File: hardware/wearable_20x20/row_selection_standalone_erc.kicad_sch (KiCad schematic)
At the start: 76 parts, among them Q201 AO3403, Q202 AO3403, Q203 AO3403, Q204 AO3403, Q205 AO3403, Q206 AO3403, Q207 AO3403, Q208 AO3403, Q209 AO3403, Q210 AO3403, Q211 AO3403, Q212 AO3403, Q213 AO3403, Q214 AO3403, Q215 AO3403, Q216 AO3403, Q217 AO3403, Q218 AO3403, Q219 AO3403, Q220 AO3403, U201 SN74LVC8T245RHLR, U202 74HC154PW,118, U203 74HC154PW,118

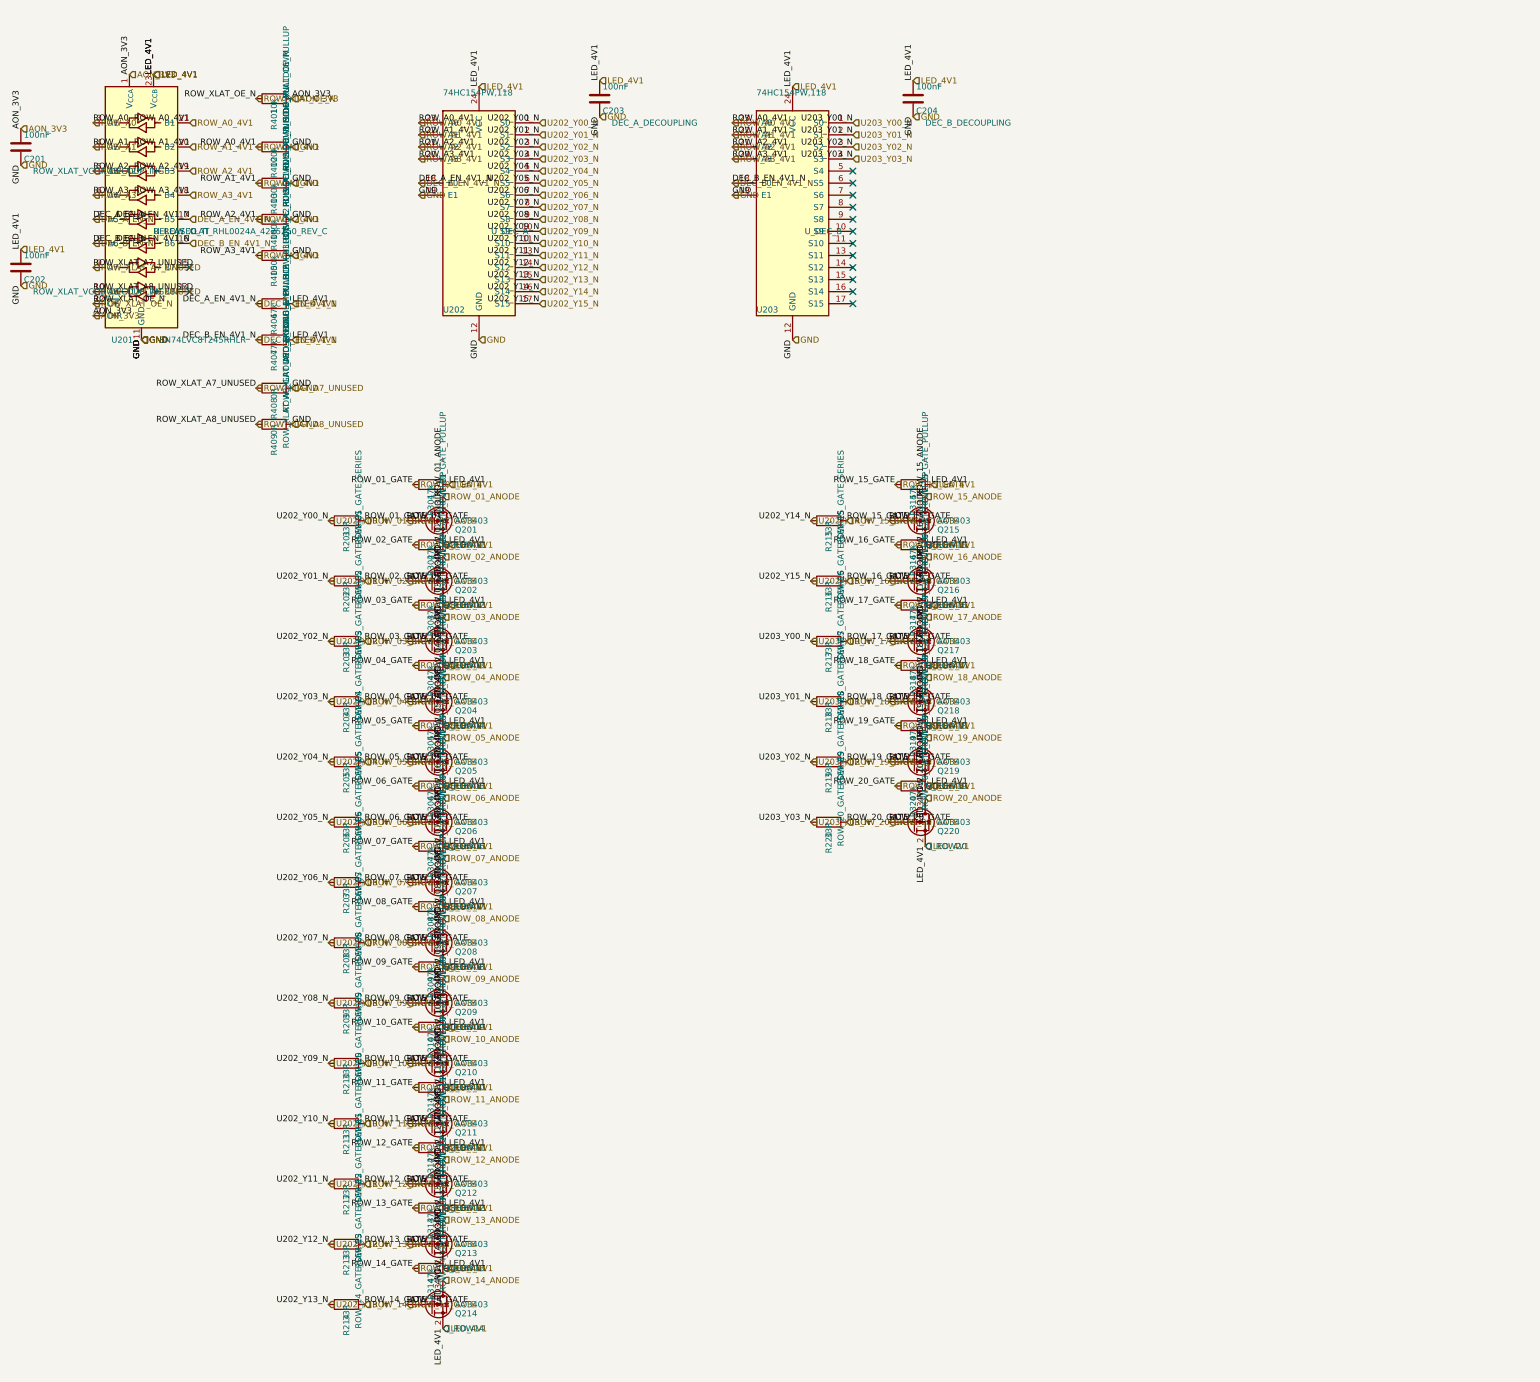
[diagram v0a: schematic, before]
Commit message: Generate complete conditional schematic hierarchy
Co-authored-by: illiapliukhin <illiapliukhin@users.noreply.github.com>
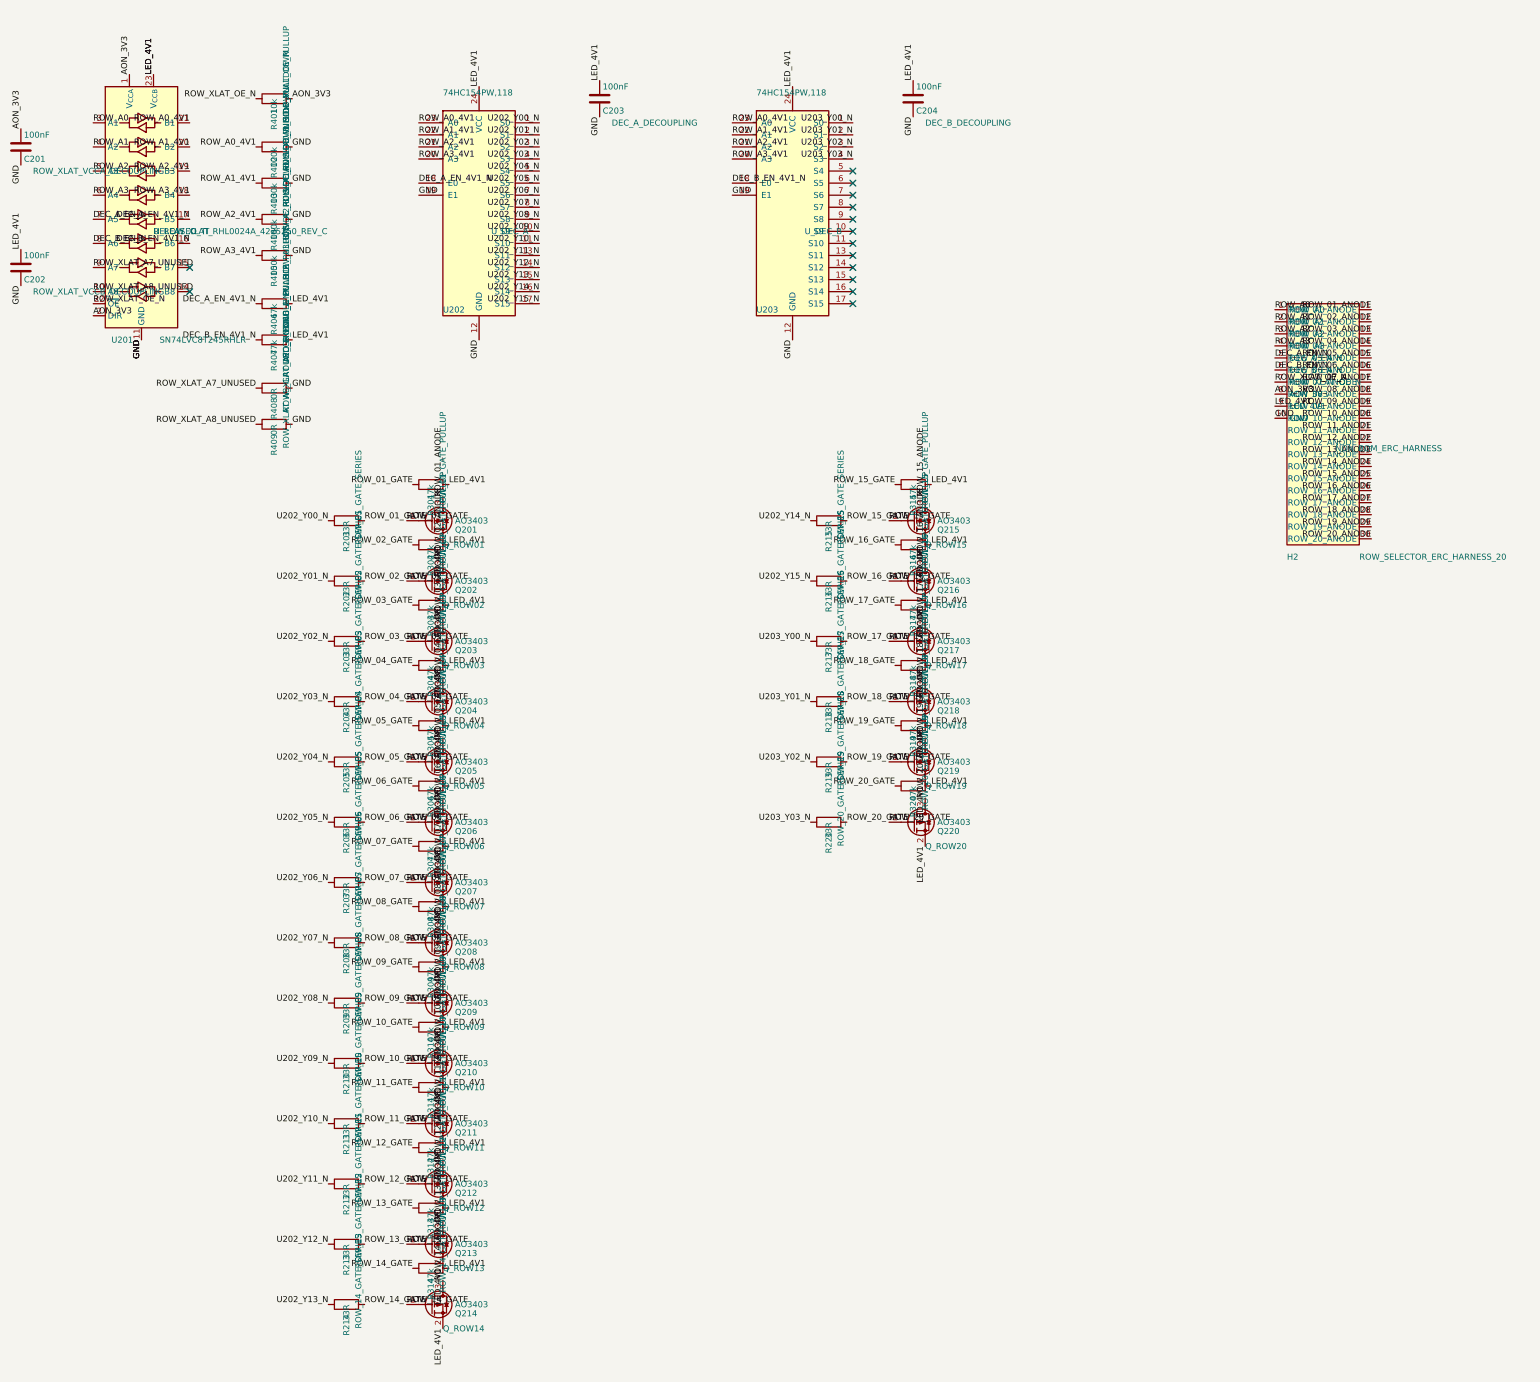
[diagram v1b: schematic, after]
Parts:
- added H2: ROW_SELECTOR_ERC_HARNESS_20, symbol PartSignal_Wearable:ROW_SELECTOR_ERC_HARNESS_20
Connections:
- net AON_3V3: now also H2.8 (AON_3V3)
- net DEC_A_EN_N: now also H2.5 (DEC_A_EN_N)
- net DEC_B_EN_N: now also H2.6 (DEC_B_EN_N)
- net GND: now also H2.10 (GND)
- net LED_4V1: now also H2.9 (LED_4V1)
- net ROW_01_ANODE: now also H2.11 (ROW_01_ANODE)
- net ROW_02_ANODE: now also H2.12 (ROW_02_ANODE)
- net ROW_03_ANODE: now also H2.13 (ROW_03_ANODE)
- net ROW_04_ANODE: now also H2.14 (ROW_04_ANODE)
- net ROW_05_ANODE: now also H2.15 (ROW_05_ANODE)
- net ROW_06_ANODE: now also H2.16 (ROW_06_ANODE)
- net ROW_07_ANODE: now also H2.17 (ROW_07_ANODE)
- net ROW_08_ANODE: now also H2.18 (ROW_08_ANODE)
- net ROW_09_ANODE: now also H2.19 (ROW_09_ANODE)
- net ROW_10_ANODE: now also H2.20 (ROW_10_ANODE)
- net ROW_11_ANODE: now also H2.21 (ROW_11_ANODE)
- net ROW_12_ANODE: now also H2.22 (ROW_12_ANODE)
- net ROW_13_ANODE: now also H2.23 (ROW_13_ANODE)
- net ROW_14_ANODE: now also H2.24 (ROW_14_ANODE)
- net ROW_15_ANODE: now also H2.25 (ROW_15_ANODE)
- net ROW_16_ANODE: now also H2.26 (ROW_16_ANODE)
- net ROW_17_ANODE: now also H2.27 (ROW_17_ANODE)
- net ROW_18_ANODE: now also H2.28 (ROW_18_ANODE)
- net ROW_19_ANODE: now also H2.29 (ROW_19_ANODE)
- net ROW_20_ANODE: now also H2.30 (ROW_20_ANODE)
- net ROW_A0: now also H2.1 (ROW_A0)
- net ROW_A1: now also H2.2 (ROW_A1)
- net ROW_A2: now also H2.3 (ROW_A2)
- net ROW_A3: now also H2.4 (ROW_A3)
- net ROW_XLAT_OE_N: now also H2.7 (ROW_XLAT_OE_N)
